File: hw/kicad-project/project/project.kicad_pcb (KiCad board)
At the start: 2 copper layers, 3 parts, among them M1 ssd1306, M2 gy219

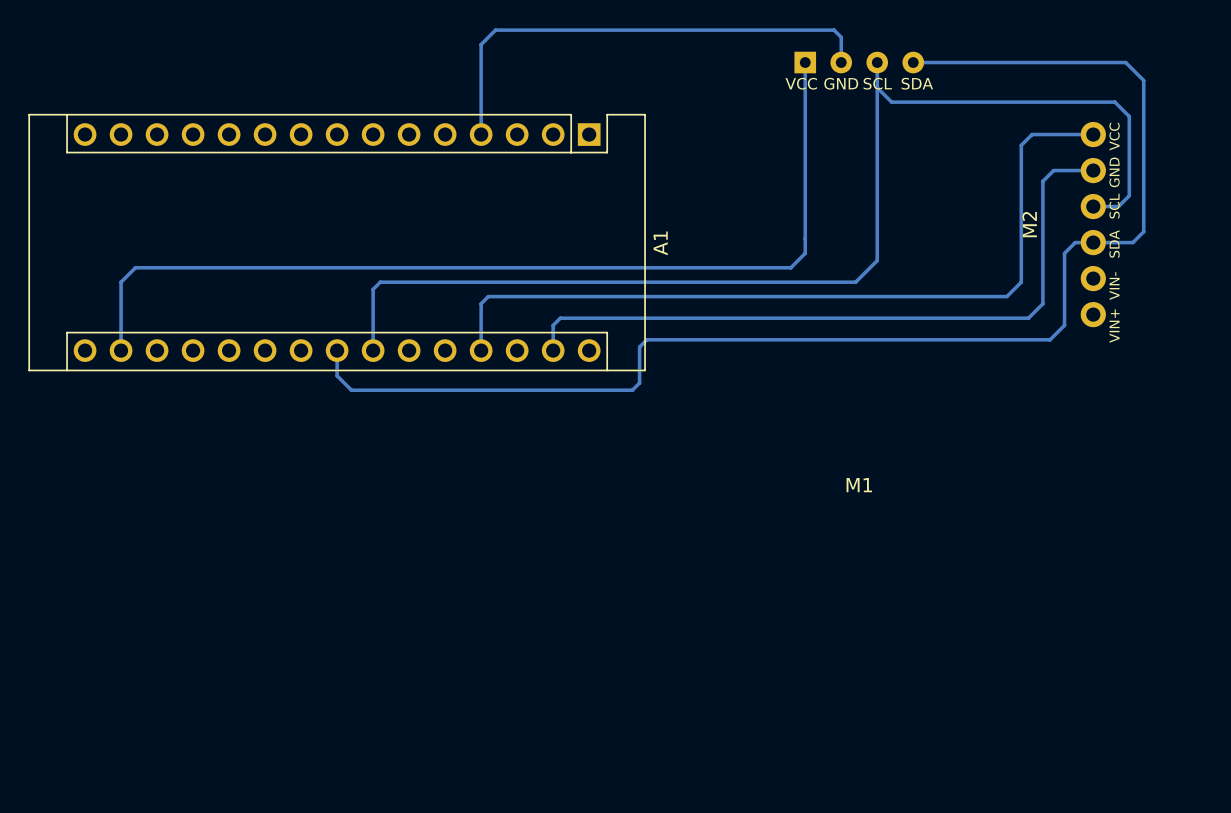
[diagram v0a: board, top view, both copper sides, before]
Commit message: hw: round cornered pcb
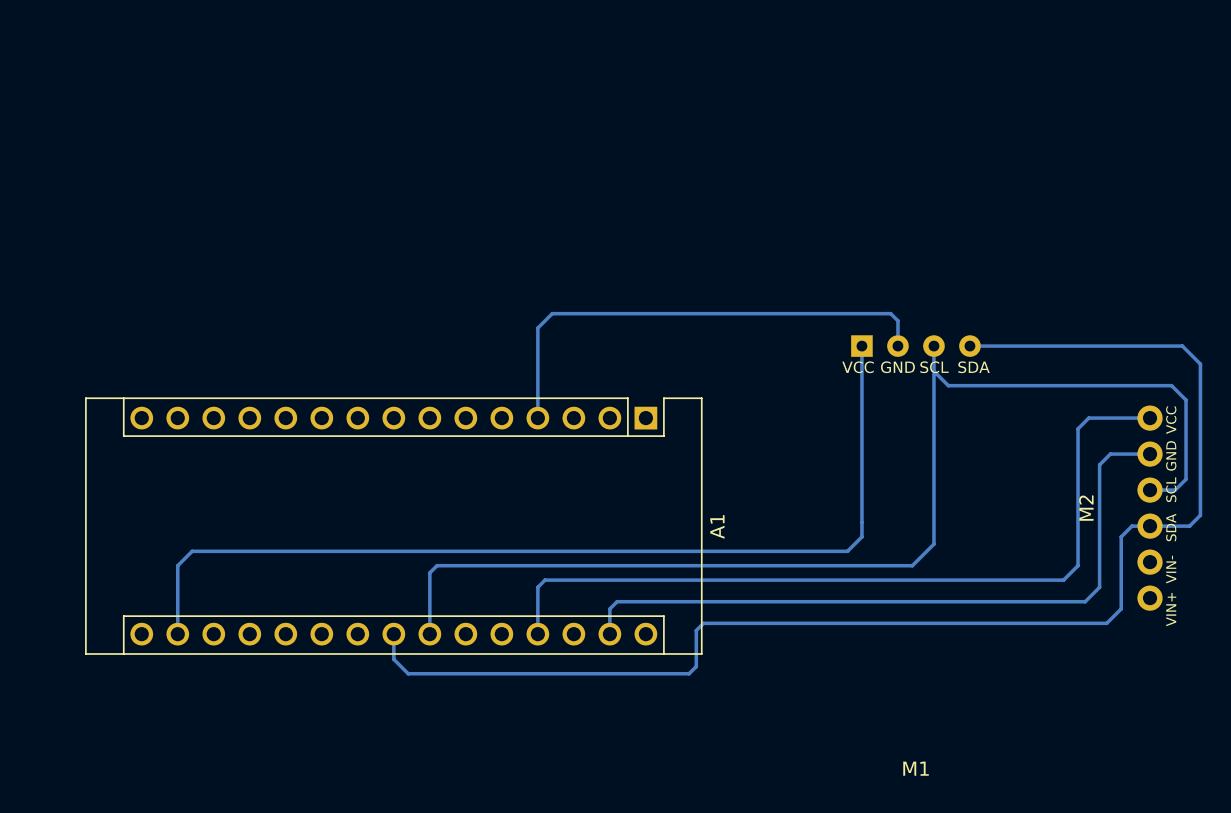
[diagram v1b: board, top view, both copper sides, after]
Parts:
- moved A1 20.4 mm to (85.3, 117.8)
- moved M1 20.4 mm to (104.3, 112.7)
- moved M2 20.4 mm to (120.8, 124.1)
